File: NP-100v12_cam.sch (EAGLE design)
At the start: 100 parts, among them IC1 LM317, IC2 LM317, IC3 LM317T, IC4 7805TV, IC5 7805TV, IC6 7812L, K1 351, Q1 2N3904, Q2 2N3904, Q3 IRF510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

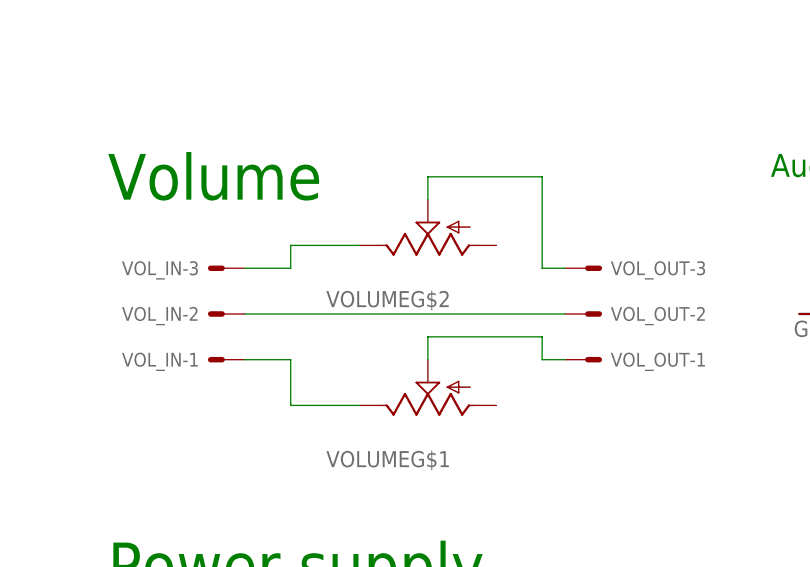
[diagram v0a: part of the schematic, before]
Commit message: - Added resistor between the wiper and ground of the volume pot
 - Added missing ground connection to the volume pot
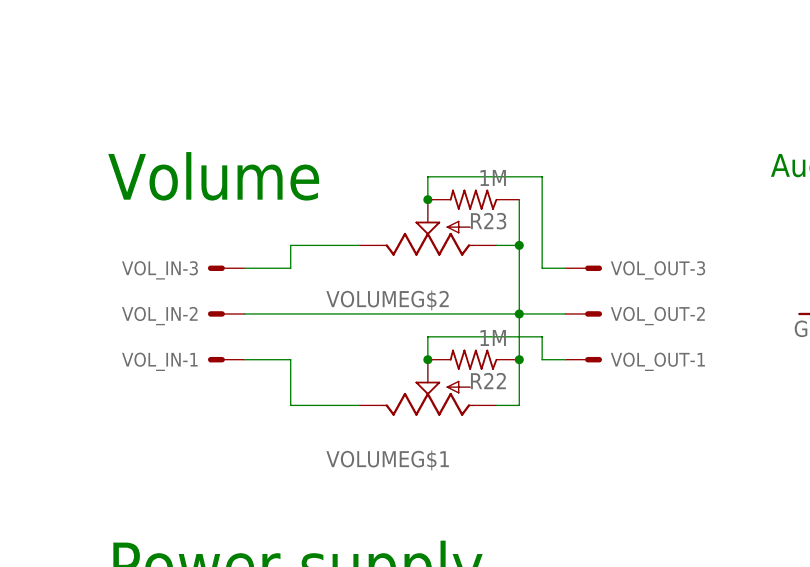
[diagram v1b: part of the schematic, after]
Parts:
- added R22, R23: 1M, adafruit:R-US_0207/10
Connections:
- net N$32: now also R22.1, R23.1, VOLUMEG$1.1, VOLUMEG$2.1
- net N$34: now also R23.2
- net N$35: now also R22.2

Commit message: - Renamed the test points to reflect their function
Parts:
- renumbered TP1 to TP_AMPPWR, TP2 to TP_GND, TP5 to TP_HTR
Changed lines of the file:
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@@
 <part name="TP3" library="testpad" deviceset="TP" device="PAD1-17"/>
 <part name="TP4" library="testpad" deviceset="TP" device="PAD1-17"/>
-<part name="TP1" library="testpad" deviceset="TP" device="PAD1-17"/>
-<part name="TP2" library="testpad" deviceset="TP" device="PAD1-17"/>
+<part name="TP_AMPPWR" library="testpad" deviceset="TP" device="PAD1-17"/>
+<part name="TP_GND" library="testpad" deviceset="TP" device="PAD1-17"/>
 <part name="C7" library="adafruit" deviceset="CPOL-US" device="E10-25" value="2200uF"/>
 <part name="C8" library="adafruit" deviceset="CPOL-US" device="E10-25" value="2200uF"/>
@@
 <part name="GND31" library="SparkFun" deviceset="GND" device=""/>
 <part name="GND32" library="SparkFun" deviceset="GND" device=""/>
-<part name="TP5" library="testpad" deviceset="TP" device="PAD1-17"/>
+<part name="TP_HTR" library="testpad" deviceset="TP" device="PAD1-17"/>
 <part name="IC4" library="linear" deviceset="78*" device="TV" technology="05"/>
 <part name="R22" library="adafruit" deviceset="R-US_" device="0207/10" value="1M"/>
@@
 <instance part="TP3" gate="G$1" x="7.62" y="60.96" rot="R270"/>
 <instance part="TP4" gate="G$1" x="177.8" y="60.96" rot="R270"/>
-<instance part="TP1" gate="G$1" x="60.96" y="-71.12"/>
-<instance part="TP2" gate="G$1" x="60.96" y="-86.36" rot="R180"/>
+<instance part="TP_AMPPWR" gate="G$1" x="60.96" y="-71.12"/>
+<instance part="TP_GND" gate="G$1" x="60.96" y="-86.36" rot="R180"/>
 <instance part="C7" gate="G$1" x="-25.4" y="-83.82"/>
 <instance part="C8" gate="G$1" x="-17.78" y="-83.82"/>
@@
 <instance part="GND31" gate="1" x="73.66" y="7.62"/>
 <instance part="GND32" gate="1" x="0" y="-208.28"/>
-<instance part="TP5" gate="G$1" x="152.4" y="-71.12"/>
+<instance part="TP_HTR" gate="G$1" x="152.4" y="-71.12"/>
 <instance part="IC4" gate="A1" x="129.54" y="-157.48"/>
 <instance part="R22" gate="G$1" x="-40.64" y="-35.56" rot="R180"/>
@@
 <wire x1="60.96" y1="-81.28" x2="55.88" y2="-81.28" width="0.1524" layer="91"/>
 <wire x1="55.88" y1="-81.28" x2="55.88" y2="-93.98" width="0.1524" layer="91"/>
-<pinref part="TP2" gate="G$1" pin="TP"/>
+<pinref part="TP_GND" gate="G$1" pin="TP"/>
 <wire x1="60.96" y1="-83.82" x2="60.96" y2="-81.28" width="0.1524" layer="91"/>
 <pinref part="PSU_AMP_OUT" gate="-1" pin="S"/>
@@
 <pinref part="F1" gate="1" pin="2"/>
 <wire x1="50.8" y1="-76.2" x2="60.96" y2="-76.2" width="0.1524" layer="91"/>
-<pinref part="TP1" gate="G$1" pin="TP"/>
+<pinref part="TP_AMPPWR" gate="G$1" pin="TP"/>
 <wire x1="60.96" y1="-73.66" x2="60.96" y2="-76.2" width="0.1524" layer="91"/>
 <pinref part="PSU_AMP_OUT" gate="-2" pin="S"/>
@@
 <pinref part="PSU_HEATER_OUT" gate="-2" pin="S"/>
 <wire x1="142.24" y1="-76.2" x2="152.4" y2="-76.2" width="0.1524" layer="91"/>
-<pinref part="TP5" gate="G$1" pin="TP"/>
+<pinref part="TP_HTR" gate="G$1" pin="TP"/>
 <wire x1="152.4" y1="-76.2" x2="154.94" y2="-76.2" width="0.1524" layer="91"/>
 <wire x1="152.4" y1="-73.66" x2="152.4" y2="-76.2" width="0.1524" layer="91"/>
